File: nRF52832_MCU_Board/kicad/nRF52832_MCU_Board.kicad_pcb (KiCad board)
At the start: 2 copper layers, 75 x 40 mm, 34 parts, among them J6 DEBUG_CONNECTOR, J7 CONN_01X05, J8 MM8130-2600, X1 32MHz, X2 32.768kHz

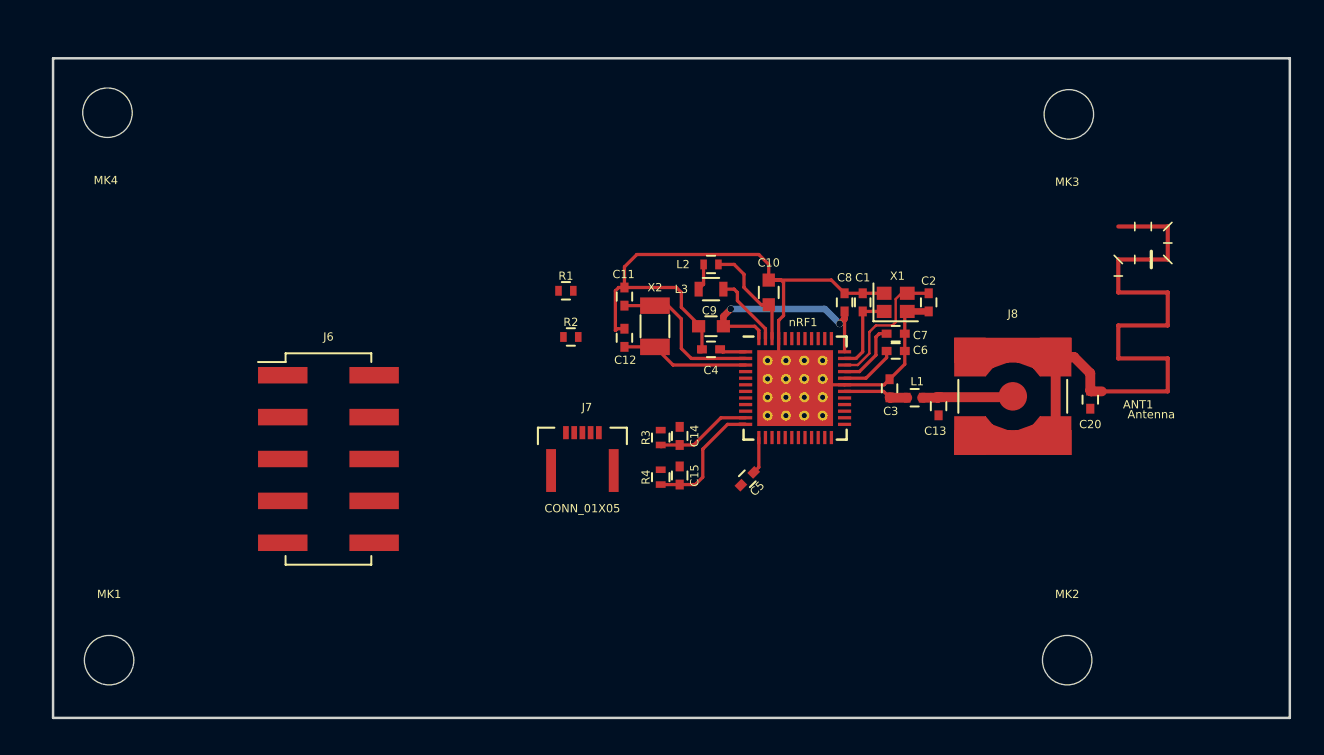
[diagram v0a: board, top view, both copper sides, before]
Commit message: Update KiCad Projec nRF52832_MCU_Board
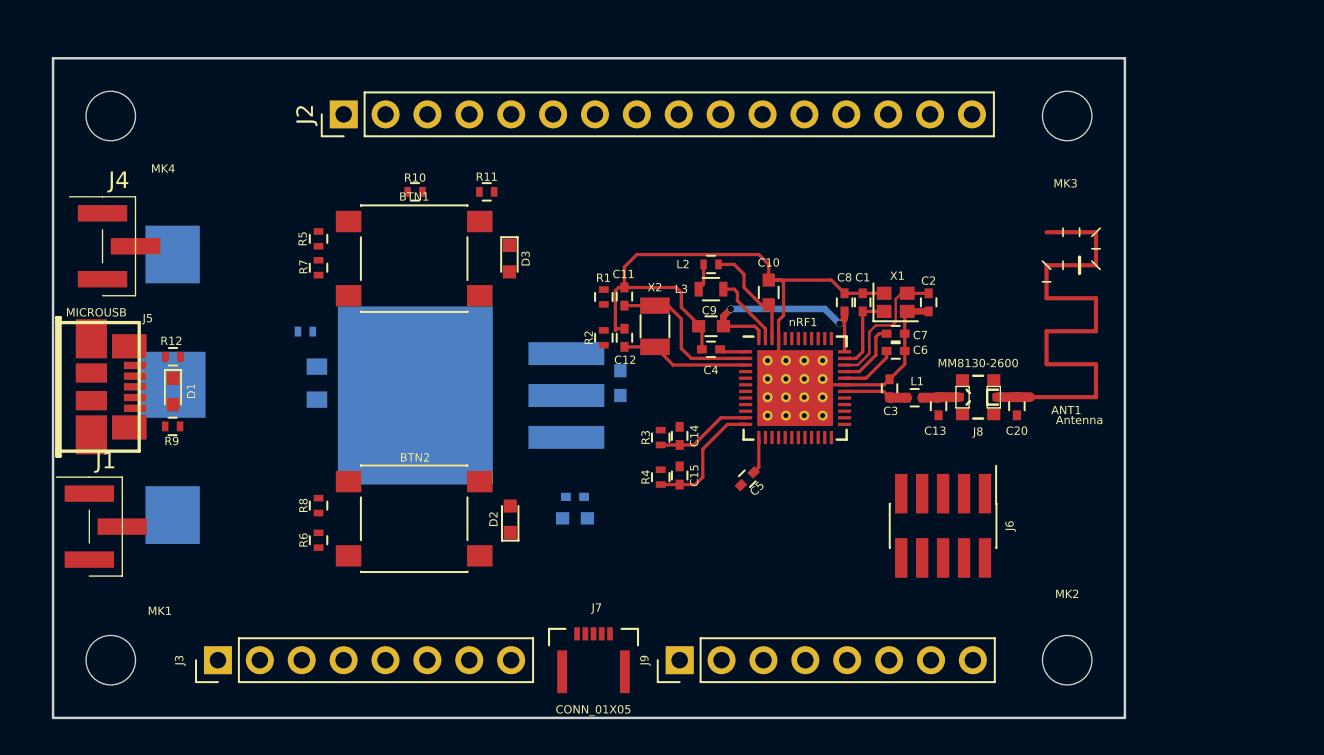
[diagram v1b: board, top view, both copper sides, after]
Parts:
- added BATT1: CR1632, Nordic_misc:keystone_3000, B.Cu at (62.2, 99.8)
- added BTN1: PANASONIC_EVQPT5A15, Buttons_Switches_SMD:SW_SPST_PTS645, F.Cu at (76.9, 92.2)
- added BTN2: PANASONIC_EVQPT5A15, Buttons_Switches_SMD:SW_SPST_PTS645, F.Cu at (76.9, 107.9)
- added C16: 100nF, Capacitors_SMD:C_0402, B.Cu at (86.7, 106.6)
- added C17: 10uF, Capacitors_SMD:C_0603, B.Cu at (86.7, 107.9)
- added C18: 10uF, Capacitors_SMD:C_0603, B.Cu at (89.4, 99.7)
- added C19: 100uF, Capacitors_SMD:C_0805, B.Cu at (71.0, 99.7)
- added D1: LED, LEDs:LED_0603, F.Cu at (62.3, 100.2)
- added D2: LED, LEDs:LED_0603, F.Cu at (82.7, 108.0)
- added D3: LED, LEDs:LED_0603, F.Cu at (82.7, 92.2)
- added J1: CONN_01X03, Pin_Headers:Pin_Header_Straight_1x03_Pitch2.54mm_SMD_Pin1Left, F.Cu at (58.2, 108.4)
- added J2: CONN_01X16, Pin_Headers:Pin_Header_Straight_1x16_Pitch2.54mm, F.Cu at (72.6, 83.4)
- added J3: CONN_01X08, Pin_Headers:Pin_Header_Straight_1x08_Pitch2.54mm, F.Cu at (65.0, 116.5)
- added J4: CONN_01X03, Pin_Headers:Pin_Header_Straight_1x03_Pitch2.54mm_SMD_Pin1Left, F.Cu at (59.0, 91.4)
- added J5: MICROUSB, Nordic_misc:conn_usb_B_micro_smd, F.Cu at (57.3, 99.9)
- added J9: CONN_01X08, Pin_Headers:Pin_Header_Straight_1x08_Pitch2.54mm, F.Cu at (93.0, 116.5)
- added R10: 330, Resistors_SMD:R_0402, F.Cu at (77.0, 88.1)
- added R11: 330, Resistors_SMD:R_0402, F.Cu at (81.3, 88.1)
- added R12: 0, Resistors_SMD:R_0402, F.Cu at (62.3, 98.1)
- added R13: 0, Resistors_SMD:R_0402, B.Cu at (70.3, 96.6)
- added R5: 330, Resistors_SMD:R_0402, F.Cu at (71.1, 91.0)
- added R6: 330, Resistors_SMD:R_0402, F.Cu at (71.1, 109.2)
- added R7: 100k, Resistors_SMD:R_0402, F.Cu at (71.1, 92.7)
- added R8: 100k, Resistors_SMD:R_0402, F.Cu at (71.1, 107.1)
- added R9: 330, Resistors_SMD:R_0402, F.Cu at (62.2, 102.3)
- added U2: TLV1117, TO_SOT_Packages_SMD:TO-263-3Lead, B.Cu at (81.5, 100.5)
- J6: footprint Pin_Headers:Pin_Header_Straight_2x05_Pitch2.54mm_SMD -> Nordic_misc:Pin_Header_Straight_2x05_Pitch1.27mm_SMD
- J8: footprint Connectors:SMA_SMD_Jack_Straight -> Nordic_misc:Nordic_misc-MM8130-2600
- moved J6 37.5 mm to (109.0, 108.3), turned to 270 degrees
- moved J7 12.2 mm to (87.8, 116.5)
- moved C20 4.47 mm to (113.5, 101.1)
- moved ANT1 4.36 mm to (114.2, 100.5)
- moved R1 2.33 mm to (88.4, 94.5), turned to 270 degrees
- moved J8 2.10 mm to (111.1, 100.5), turned to 90 degrees
- moved R2 2.00 mm to (88.4, 97.0), turned to 90 degrees
- moved MK4 0.28 mm to (58.5, 83.5)
- moved MK3 0.14 mm to (116.5, 83.5)
- moved MK1 0.10 mm to (58.5, 116.5)
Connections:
- net /nRF528323_MCU/P0.18/SWO/2.2B renamed /P0.18
- net /nRF528323_MCU/P0.21/RESET/2.2B renamed /P0.21
- R1 pad 1: /nRF528323_MCU/P0.00/2.2A -> /P0.00
- R2 pad 2: /nRF528323_MCU/P0.01/2.2A -> /P0.01
- R3 pad 1: /nRF528323_MCU/P0.09/2.2B -> /P0.09
- R4 pad 2: /nRF528323_MCU/P0.10/2.2B -> /P0.10
- nRF1 pad 10: /nRF528323_MCU/P0.08/2.2A -> /P0.08
- nRF1 pad 14: /nRF528323_MCU/P0.11/2.2B -> /P0.11
- nRF1 pad 15: /nRF528323_MCU/P0.12/2.2B -> /P0.12
- nRF1 pad 16: /nRF528323_MCU/P0.13/2.2B -> /P0.13
- nRF1 pad 17: /nRF528323_MCU/P0.14/2.2B -> /P0.14
- nRF1 pad 18: /nRF528323_MCU/P0.15/2.2B -> /P0.15
- nRF1 pad 19: /nRF528323_MCU/P0.16/2.2B -> /P0.16
- nRF1 pad 20: /nRF528323_MCU/P0.17/2.2B -> /P0.17
- nRF1 pad 22: /nRF528323_MCU/P0.19/2.2B -> /P0.19
- nRF1 pad 23: /nRF528323_MCU/P0.20/2.2B -> /P0.20
- nRF1 pad 27: /nRF528323_MCU/P0.22/2.2B -> /P0.22
- nRF1 pad 28: /nRF528323_MCU/P0.23/2.2B -> /P0.23
- nRF1 pad 29: /nRF528323_MCU/P0.24/2.2B -> /P0.24
- nRF1 pad 37: /nRF528323_MCU/P0.25/2.2A -> /P0.25
- nRF1 pad 38: /nRF528323_MCU/P0.26/2.2A -> /P0.26
- nRF1 pad 39: /nRF528323_MCU/P0.27/2.2A -> /P0.27
- nRF1 pad 4: /nRF528323_MCU/P0.02/2.2A -> /P0.02
- nRF1 pad 40: /nRF528323_MCU/P0.28/2.2A -> /P0.28
- nRF1 pad 41: /nRF528323_MCU/P0.29/2.2A -> /P0.29
- nRF1 pad 42: /nRF528323_MCU/P0.30/2.2A -> /P0.30
- nRF1 pad 43: /nRF528323_MCU/P0.31/2.2A -> /P0.31
- nRF1 pad 5: /nRF528323_MCU/P0.03/2.2A -> /P0.03
- nRF1 pad 6: /nRF528323_MCU/P0.04/2.2A -> /P0.04
- nRF1 pad 7: /nRF528323_MCU/P0.05/2.2A -> /P0.05
- nRF1 pad 8: /nRF528323_MCU/P0.06/2.2A -> /P0.06
- nRF1 pad 9: /nRF528323_MCU/P0.07/2.2A -> /P0.07
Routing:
- net Net-(ANT1-Pad1): track 9.18 -> 1.99 mm
- net Net-(C13-Pad2): track 5.53 -> 2.25 mm
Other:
- board size 75 x 40 mm -> 65 x 40 mm
- net class GROUND added: clearance 0.15, trace_width 0.2, via_dia 0.8, via_drill 0.4

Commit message: Update KiCad project nRF52832_MCU_Board
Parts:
- J2: footprint Pin_Headers:Pin_Header_Straight_1x16_Pitch2.54mm -> Nordic_misc:Pin_Header_Straight_1x16_Pitch2.54mm
- J3, J9: footprint Pin_Headers:Pin_Header_Straight_1x08_Pitch2.54mm -> Nordic_misc:Pin_Header_Straight_1x08_Pitch2.54mm

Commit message: Update KiCad Project nRF52832_MCU_Board
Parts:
- J1, J4: footprint Pin_Headers:Pin_Header_Straight_1x03_Pitch2.54mm_SMD_Pin1Left -> Nordic_misc:bb02-hy03a
- J2: footprint Nordic_misc:Pin_Header_Straight_1x16_Pitch2.54mm -> Nordic_misc:bb02-hy16a
- J3, J9: footprint Nordic_misc:Pin_Header_Straight_1x08_Pitch2.54mm -> Nordic_misc:bb02-hy08a
- J6: footprint Nordic_misc:Pin_Header_Straight_2x05_Pitch1.27mm_SMD -> Nordic_misc:ftsh-105-01-l-dv
- moved J2 20.1 mm to (92.7, 83.5), turned to 180 degrees
- moved J9 9.80 mm to (102.8, 116.5), turned to 0 degrees
- moved J3 9.60 mm to (74.6, 116.5), turned to 0 degrees
- moved U2 6.43 mm to (77.0, 105.0)
- moved R10 3.67 mm to (79.2, 91.0)
- moved R6 3.63 mm to (70.9, 105.6)
- moved R8 3.53 mm to (71.0, 103.6)
- moved R7 3.50 mm to (71.1, 96.2)
- moved R5 3.45 mm to (71.1, 94.4)
- moved D3 3.25 mm to (82.8, 95.4)
- moved BTN2 2.92 mm to (76.9, 105.0)
- moved R11 2.92 mm to (81.0, 91.0)
- moved BTN1 2.85 mm to (77.0, 95.0)
- moved D2 2.78 mm to (83.1, 105.2)
- moved J7 0.52 mm to (88.3, 116.5)
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
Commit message: Update KiCAD Project nRF52832_MCU_Board
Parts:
- D1, D2, D3: footprint LEDs:LED_0603 -> Nordic_misc:LED_0603
- X1: footprint Crystals:Crystal_SMD_2016-4pin_2.0x1.6mm -> Nordic_nRF:Crystal_SMD_2016-4pin_2.0x1.6mm
- X2: footprint Crystals:Crystal_SMD_3215-2pin_3.2x1.5mm -> Nordic_nRF:Crystal_SMD_3215-2pin_3.2x1.5mm

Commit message: Update KiCAD Project nRF52832_MCU_Board
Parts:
- J1, J4: footprint Nordic_misc:bb02-hy03a -> Nordic_misc:Pin_Header_Straight_1x03_Pitch2.54mm
- J6: value DEBUG_CONNECTOR -> CONN_02X05
- nRF1: footprint nRF52:UQFN-48-1EP_6x6mm_Pitch0.4mm -> Nordic_nRF:Nordic_nRF-QFN40P600X600X90-48_N
- moved U2 6.70 mm to (81.5, 100.0)
- moved J1 4.90 mm to (62.0, 111.5), turned to 270 degrees
- moved J4 3.77 mm to (56.9, 88.3)
- moved C18 1.66 mm to (91.0, 100.0), turned to 0 degrees
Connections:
- D1 pad 1: +5V -> (no net)
- D1 pad 2: Net-(D1-Pad2) -> (no net)
- D2 pad 1: Net-(D2-Pad1) -> (no net)
- D2 pad 2: +3V3 -> (no net)
- D3 pad 1: Net-(D3-Pad1) -> (no net)
- D3 pad 2: +3V3 -> (no net)
- J5 pad 2: Net-(J5-Pad2) -> (no net)
- J5 pad 3: Net-(J5-Pad3) -> (no net)
- J5 pad 4: Net-(J5-Pad4) -> (no net)
- J6 pad 1: +3V3 -> /nRF528323_MCU/SWDIO
- J6 pad 10: /P0.21 -> GND
- J6 pad 2: /nRF528323_MCU/SWDIO -> +3V3
- J6 pad 3: Net-(J6-Pad3) -> /nRF528323_MCU/SWCLK
- J6 pad 4: /nRF528323_MCU/SWCLK -> (no net)
- J6 pad 5: GND -> /P0.18
- J6 pad 6: /P0.18 -> GND
- J6 pad 7: Net-(J6-Pad7) -> (no net)
- J6 pad 8: Net-(J6-Pad8) -> (no net)
- J6 pad 9: GND -> /P0.21
- J7 pad 1: Net-(J7-Pad1) -> (no net)
- J7 pad 3: Net-(J7-Pad3) -> (no net)
- J7 pad 5: Net-(J7-Pad5) -> (no net)
- J8 pad 1: Net-(C13-Pad2) -> (no net)
- J8 pad 2: Net-(ANT1-Pad1) -> (no net)
- R10 pad 1: Net-(D2-Pad1) -> (no net)
- R11 pad 1: Net-(D3-Pad1) -> (no net)
- R9 pad 1: Net-(D1-Pad2) -> (no net)
- nRF1 pad 44: Net-(nRF1-Pad44) -> (no net)

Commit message: Update KiCAD Project nRF52832_MCU_Board
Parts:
- BATT1: footprint Nordic_misc:keystone_3000 -> Nordic_misc:Keystone_1058_1x2032-CoinCell
- moved C17 14.9 mm to (79.6, 94.8), turned to 90 degrees
- moved C16 11.7 mm to (80.9, 96.4), turned to 90 degrees
- moved U2 10.7 mm to (87.2, 91.0), turned to 90 degrees
- moved C19 10.6 mm to (81.3, 102.0)
- moved R13 10.5 mm to (79.0, 90.6)
- moved BATT1 4.86 mm to (67.1, 99.1)
- moved C18 3.25 mm to (87.8, 100.1)
- moved J4 0.65 mm to (56.3, 88.5)
- moved J1 0.42 mm to (61.6, 111.4)

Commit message: Update KiCAD Project nRF52832_MCU_Board
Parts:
- BTN1, BTN2: footprint Buttons_Switches_SMD:SW_SPST_PTS645 -> Nordic_misc:Nordic_misc-PANASONIC_EVQPT5A15
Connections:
- BTN2 pad 2: Net-(BTN2-Pad2) -> (no net)

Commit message: Update  KiCAD Project nRF52832_MCU_Board
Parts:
- removed BTN1, BTN2: PANASONIC_EVQPT5A15, Nordic_misc:Nordic_misc-PANASONIC_EVQPT5A15
- added SW1: SW_SPST, Nordic_misc:SW_SPST_FSMSM, F.Cu at (77.3, 96.0)
- added SW2: SW_SPST, Nordic_misc:SW_SPST_FSMSM, F.Cu at (77.8, 104.6)
- BATT1: footprint Nordic_misc:Keystone_1058_1x2032-CoinCell -> w_battery_holders:keystone_3000
- J2: footprint Nordic_misc:bb02-hy16a -> Nordic_misc:Pin_Header_Straight_1x16_Pitch2.54mm
- J3, J9: footprint Nordic_misc:bb02-hy08a -> Nordic_misc:Pin_Header_Straight_1x08_Pitch2.54mm
- U2: footprint TO_SOT_Packages_SMD:TO-263-3Lead -> TO_SOT_Packages_SMD:SOT-223-3Lead_TabPin2
- moved J2 19.5 mm to (73.3, 81.8), turned to 90 degrees
- moved C18 18.9 mm to (69.6, 105.2)
- moved R5 17.6 mm to (86.9, 102.1), turned to 180 degrees
- moved U2 15.4 mm to (74.8, 100.2), turned to 0 degrees
- moved R7 14.2 mm to (84.3, 101.4), turned to 270 degrees
- moved R10 13.9 mm to (89.2, 100.7)
- moved R13 13.7 mm to (69.1, 100.2)
- moved C16 12.2 mm to (68.8, 95.4)
- moved R11 11.6 mm to (89.1, 99.2)
- moved R6 11.5 mm to (82.1, 108.3), turned to 180 degrees
- moved R8 10.1 mm to (79.9, 108.3), turned to 0 degrees
- moved J4 9.82 mm to (63.7, 82.0)
- moved J9 8.53 mm to (111.3, 117.2), turned to 270 degrees
- moved J3 7.66 mm to (82.2, 117.2), turned to 270 degrees
- moved J1 6.56 mm to (68.1, 112.2)
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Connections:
- D1 pad 1: (no net) -> Net-(D1-Pad1)
- D1 pad 2: (no net) -> +5V
- D2 pad 1: (no net) -> +3V3
- D2 pad 2: (no net) -> Net-(D2-Pad2)
- D3 pad 1: (no net) -> +3V3
- D3 pad 2: (no net) -> Net-(D3-Pad2)
- J2 pad 1: /P0.09 -> /P0.08
- J2 pad 10: /P0.18 -> /P0.31
- J2 pad 11: /P0.19 -> /P0.30
- J2 pad 12: /P0.20 -> /P0.29
- J2 pad 13: /P0.21 -> /P0.28
- J2 pad 14: /P0.22 -> /P0.27
- J2 pad 15: /P0.23 -> /P0.26
- J2 pad 16: /P0.24 -> /P0.25
- J2 pad 2: /P0.10 -> /P0.07
- J2 pad 3: /P0.11 -> /P0.06
- J2 pad 4: /P0.12 -> /P0.05
- J2 pad 5: /P0.13 -> /P0.04
- J2 pad 6: /P0.14 -> /P0.03
- J2 pad 7: /P0.15 -> /P0.02
- J2 pad 8: /P0.16 -> /P0.01
- J2 pad 9: /P0.17 -> /P0.00
- J3 pad 1: /P0.01 -> /P0.16
- J3 pad 2: /P0.02 -> /P0.15
- J3 pad 3: /P0.03 -> /P0.14
- J3 pad 4: /P0.04 -> /P0.13
- J3 pad 5: /P0.05 -> /P0.12
- J3 pad 6: /P0.06 -> /P0.11
- J3 pad 7: /P0.07 -> /P0.10
- J3 pad 8: /P0.08 -> /P0.09
- J8 pad 1: (no net) -> Net-(C13-Pad2)
- J8 pad 2: (no net) -> Net-(ANT1-Pad1)
- J9 pad 1: /P0.25 -> /P0.24
- J9 pad 2: /P0.26 -> /P0.23
- J9 pad 3: /P0.27 -> /P0.22
- J9 pad 4: /P0.28 -> /P0.21
- J9 pad 5: /P0.29 -> /P0.20
- J9 pad 6: /P0.30 -> /P0.19
- J9 pad 7: /P0.31 -> /P0.18
- J9 pad 8: /P0.00 -> /P0.17
- R10 pad 1: (no net) -> Net-(D2-Pad2)
- R11 pad 1: (no net) -> Net-(D3-Pad2)
- R9 pad 1: (no net) -> Net-(D1-Pad1)
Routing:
- net GND: track 84.7 -> 276.5 mm, vias 0 -> 9
- net +3V3: track 16.5 -> 125.6 mm, vias 2 -> 9
- net +5V: track 0.00 -> 44.4 mm, vias 0 -> 2
- net /P0.21: track 0.00 -> 41.4 mm, vias 0 -> 3
- net /P0.08: track 0.00 -> 39.5 mm, vias 0 -> 1
- net /P0.10: track 0.00 -> 37.1 mm, vias 0 -> 1
- net /P0.09: track 0.00 -> 36.8 mm, vias 0 -> 1
- net /P0.11: track 0.00 -> 36.5 mm, vias 0 -> 1
- net /P0.07: track 0.00 -> 35.6 mm, vias 0 -> 1
- net /P0.12: track 0.00 -> 34.8 mm, vias 0 -> 1
- net /P0.13: track 0.00 -> 33.0 mm, vias 0 -> 1
- net /P0.06: track 0.00 -> 31.5 mm, vias 0 -> 1
- net /P0.14: track 0.00 -> 30.5 mm, vias 0 -> 1
- net /P0.05: track 0.00 -> 28.3 mm, vias 0 -> 1
- net /P0.15: track 0.00 -> 28.1 mm, vias 0 -> 1
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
